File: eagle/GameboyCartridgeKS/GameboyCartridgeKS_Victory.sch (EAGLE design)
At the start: 4 parts, among them IC1 AT49F040J

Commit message: Victory version of 32kb GB cartridge draft done, pending review.
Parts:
- removed R1: 47K, resistor:R-US_M0805
- added C2: 10uF, SparkFun-Capacitors:10UF-1206-6.3V-20%
- added JP1, JP2, JP3, JP4: JUMPER-SMT_2_NC_TRACE_SILK, SparkFun-Jumpers:JUMPER-SMT_2_NC_TRACE_SILK
- added TP1, TP2, TP3, TP4, TP5, TP6, TP7, TP8: TEST-POINT3X5, SparkFun-Connectors:TEST-POINT3X5
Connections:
- removed net A: IC1.A18
- removed net B: IC1.A17
- removed net C: IC1.A16
- removed net D: IC1.A15
- removed net E: IC1.A14
- new net N$1: IC1.!WE, JP4.2, TP1.1
- new net N$5: IC1.A16, JP1.2, TP2.1
- new net N$6: IC1.A17, JP2.2, TP3.1
- new net N$7: IC1.A18, JP3.2, TP4.1
- net 20: now also IC1.A14
- net 21: now also IC1.A15; no longer IC1.!CE
- net 30: now also TP8.1
- net 31: now also TP7.1; no longer IC1.!WE, R1.1
- net GND: now also C2.2, IC1.!CE, JP1.1, JP2.1, TP5.1
- net VDD: now also C2.1, JP3.1, JP4.1, TP6.1; no longer R1.2
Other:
- note added: "Pin 1 = /RESET"
- moved on the sheet: IC1

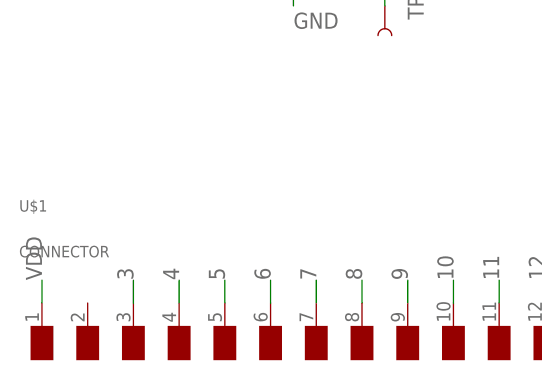
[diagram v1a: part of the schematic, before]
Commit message: New Pigman logo, Victory GB cartridge in last round of review
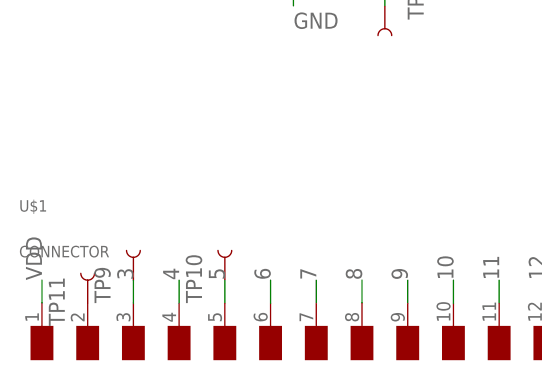
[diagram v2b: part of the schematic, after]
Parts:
- added TP10, TP11, TP9: TEST-POINT3X5, SparkFun-Connectors:TEST-POINT3X5
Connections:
- new net N$2: TP11.1, U$1.NC
- net 3: now also TP9.1
- net 5: now also TP10.1
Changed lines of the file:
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@@
 <part name="TP7" library="SparkFun-Connectors" library_urn="urn:adsk.eagle:library:513" deviceset="TEST-POINT" device="3X5" package3d_urn="urn:adsk.eagle:package:38285/1"/>
 <part name="TP8" library="SparkFun-Connectors" library_urn="urn:adsk.eagle:library:513" deviceset="TEST-POINT" device="3X5" package3d_urn="urn:adsk.eagle:package:38285/1"/>
+<part name="TP9" library="SparkFun-Connectors" library_urn="urn:adsk.eagle:library:513" deviceset="TEST-POINT" device="3X5" package3d_urn="urn:adsk.eagle:package:38285/1"/>
+<part name="TP10" library="SparkFun-Connectors" library_urn="urn:adsk.eagle:library:513" deviceset="TEST-POINT" device="3X5" package3d_urn="urn:adsk.eagle:package:38285/1"/>
+<part name="TP11" library="SparkFun-Connectors" library_urn="urn:adsk.eagle:library:513" deviceset="TEST-POINT" device="3X5" package3d_urn="urn:adsk.eagle:package:38285/1"/>
 </parts>
 <sheets>
@@
 <attribute name="VALUE" x="142.24" y="53.34" size="1.778" layer="96" font="vector" rot="R90"/>
 </instance>
+<instance part="TP9" gate="G$1" x="2.54" y="55.88" smashed="yes" rot="R90">
+<attribute name="NAME" x="0" y="53.34" size="1.778" layer="95" font="vector" rot="R90"/>
+</instance>
+<instance part="TP10" gate="G$1" x="12.7" y="55.88" smashed="yes" rot="R90">
+<attribute name="NAME" x="10.16" y="53.34" size="1.778" layer="95" font="vector" rot="R90"/>
+</instance>
+<instance part="TP11" gate="G$1" x="-2.54" y="53.34" smashed="yes" rot="R90">
+<attribute name="NAME" x="-5.08" y="50.8" size="1.778" layer="95" font="vector" rot="R90"/>
+</instance>
 </instances>
 <busses>
@@
 <wire x1="12.7" y1="53.34" x2="12.7" y2="55.88" width="0.1524" layer="91"/>
 <label x="12.7" y="55.88" size="1.778" layer="95" rot="R90"/>
+<pinref part="TP10" gate="G$1" pin="1"/>
 </segment>
 </net>
@@
 <wire x1="2.54" y1="53.34" x2="2.54" y2="55.88" width="0.1524" layer="91"/>
 <label x="2.54" y="55.88" size="1.778" layer="95" rot="R90"/>
+<pinref part="TP9" gate="G$1" pin="1"/>
 </segment>
 </net>
@@
 </segment>
 </net>
+<net name="N$2" class="0">
+<segment>
+<pinref part="U$1" gate="G$1" pin="NC"/>
+<pinref part="TP11" gate="G$1" pin="1"/>
+</segment>
+</net>

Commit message: Board GB Victory sent to prod.
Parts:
- added JP5: JUMPER-SMT_3_1-NC_TRACE_SILK, SparkFun-Jumpers:JUMPER-SMT_3_1-NC_TRACE_SILK
- added TP12: TEST-POINT3X5, SparkFun-Connectors:TEST-POINT3X5
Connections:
- new net N$3: IC1.A15, JP5.2, TP12.1
- net 21: now also JP5.1; no longer IC1.A15
- net GND: now also JP5.3
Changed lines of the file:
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@@
 <part name="TP10" library="SparkFun-Connectors" library_urn="urn:adsk.eagle:library:513" deviceset="TEST-POINT" device="3X5" package3d_urn="urn:adsk.eagle:package:38285/1"/>
 <part name="TP11" library="SparkFun-Connectors" library_urn="urn:adsk.eagle:library:513" deviceset="TEST-POINT" device="3X5" package3d_urn="urn:adsk.eagle:package:38285/1"/>
+<part name="JP5" library="SparkFun-Jumpers" deviceset="JUMPER-SMT_3_1-NC_TRACE" device="_SILK" package3d_urn="urn:adsk.eagle:package:39288/1"/>
+<part name="TP12" library="SparkFun-Connectors" library_urn="urn:adsk.eagle:library:513" deviceset="TEST-POINT" device="3X5" package3d_urn="urn:adsk.eagle:package:38285/1"/>
 </parts>
 <sheets>
@@
 <attribute name="NAME" x="-5.08" y="50.8" size="1.778" layer="95" font="vector" rot="R90"/>
 </instance>
+<instance part="JP5" gate="G$1" x="86.36" y="119.38" smashed="yes" rot="R180">
+<attribute name="NAME" x="83.82" y="118.999" size="1.778" layer="95" font="vector" rot="R180"/>
+</instance>
+<instance part="TP12" gate="G$1" x="91.44" y="119.38" smashed="yes" rot="R90">
+<attribute name="NAME" x="88.9" y="116.84" size="1.778" layer="95" font="vector" rot="R90"/>
+</instance>
 </instances>
 <busses>
@@
 </segment>
 <segment>
-<pinref part="IC1" gate="G$1" pin="A15"/>
-<wire x1="119.38" y1="99.06" x2="114.3" y2="99.06" width="0.1524" layer="91"/>
-<label x="114.3" y="99.06" size="1.778" layer="95"/>
+<pinref part="JP5" gate="G$1" pin="1"/>
+<wire x1="86.36" y1="114.3" x2="78.74" y2="114.3" width="0.1524" layer="91"/>
+<label x="76.2" y="114.3" size="1.778" layer="95"/>
 </segment>
 </net>
@@
 <wire x1="20.32" y1="91.44" x2="20.32" y2="86.36" width="0.1524" layer="91"/>
 <label x="20.32" y="83.82" size="1.778" layer="95"/>
+</segment>
+<segment>
+<pinref part="JP5" gate="G$1" pin="3"/>
+<wire x1="86.36" y1="124.46" x2="86.36" y2="127" width="0.1524" layer="91"/>
+<wire x1="86.36" y1="127" x2="78.74" y2="127" width="0.1524" layer="91"/>
+<label x="78.74" y="127" size="1.778" layer="95"/>
 </segment>
 </net>
@@
 </segment>
 </net>
+<net name="N$3" class="0">
+<segment>
+<pinref part="JP5" gate="G$1" pin="2"/>
+<wire x1="91.44" y1="119.38" x2="109.22" y2="119.38" width="0.1524" layer="91"/>
+<wire x1="109.22" y1="119.38" x2="109.22" y2="99.06" width="0.1524" layer="91"/>
+<pinref part="IC1" gate="G$1" pin="A15"/>
+<wire x1="109.22" y1="99.06" x2="119.38" y2="99.06" width="0.1524" layer="91"/>
+<pinref part="TP12" gate="G$1" pin="1"/>
+<junction x="91.44" y="119.38"/>
+</segment>
+</net>
